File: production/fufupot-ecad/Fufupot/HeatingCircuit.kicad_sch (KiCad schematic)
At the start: 0 parts

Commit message: Heating Schematic Finished
heating schematic finished
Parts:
- added C1: 3.3 uF 275V, symbol Device:C_Polarized
- added C3: 10uF 25V, symbol Device:C_Polarized
- added C4: 0.1uF 63V, symbol Device:C_Polarized
- added C5: 0.37uF 1200V, symbol Device:C_Polarized
- added IC1: FOD3150, DIP762W56P254L966H508Q8N, symbol FOD3150:FOD3150
- added L1: L, symbol Device:L
- added L2: 10uH, symbol Device:L
- added R1: 0.1 5W, symbol Device:R
- added R2: 3.3k, symbol Device:R
- added R3: 10k, symbol Device:R
- added R4: 16, symbol Device:R
- added R5: 330, symbol Device:R
- added U1: STGP8NC60KD, TO-220FP_STM, symbol STGP8NC60KD:STGP8NC60KD
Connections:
- new net: IC1.2 (ANODE), R5.2
- new net: C1.1, C5.1, L1.1, L2.2
- new net: C5.2, L1.2, U1.2 (C)
- new net: C3.2, IC1.5 (VSS), R1.1, R2.1, R3.2, U1.3 (E)
- new net: IC1.6 (VO1), IC1.7 (VO2), R4.1
- new net: R3.1, R4.2, U1.1 (G)
- new net +15V: C3.1, IC1.8 (VDD)
- new net +48V: L2.1
- new net A1: C4.1, R2.2
- new net D9: R5.1
- new net GND: C1.2, C4.2, IC1.3 (CATHODE), R1.2
- no-connect marks 0 -> 2

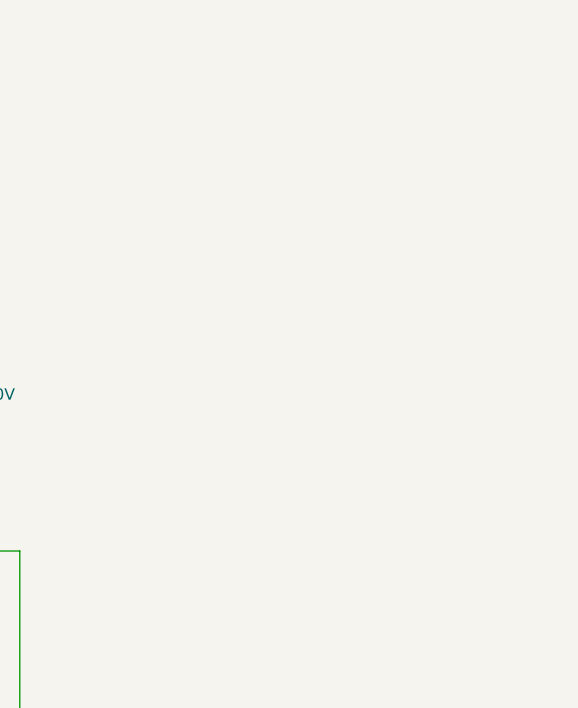
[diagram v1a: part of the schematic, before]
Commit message: Update HeatingCircuit.kicad_sch
Added temp sensing
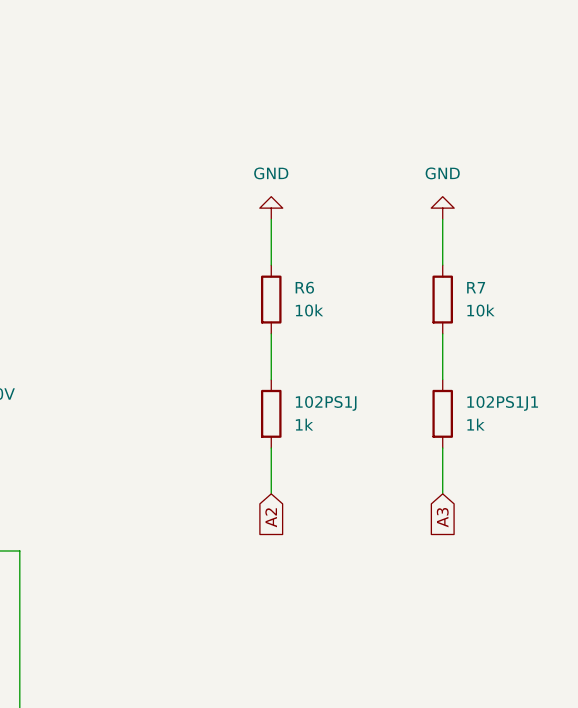
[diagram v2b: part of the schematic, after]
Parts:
- added 102PS1J, 102PS1J1: 1k, symbol Device:R
- added R6, R7: 10k, symbol Device:R
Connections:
- net GND: now also R6.1, R7.1
- new net: 102PS1J1.1, R7.2
- new net: 102PS1J.1, R6.2
- new net A2: 102PS1J.2
- new net A3: 102PS1J1.2
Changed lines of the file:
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@@
+    (stroke (width 0) (type default))
+  )
+  (wire (pts (xy 208.28 77.47) (xy 208.28 82.55))
+    (stroke (width 0) (type default))
+  )
+  (wire (pts (xy 227.33 77.47) (xy 227.33 82.55))
     (stroke (width 0) (type default))
   )
@@
     (stroke (width 0) (type default))
   )
+  (wire (pts (xy 208.28 52.07) (xy 208.28 57.15))
+    (stroke (width 0) (type default))
+  )
   (wire (pts (xy 69.85 107.95) (xy 76.2 107.95))
     (stroke (width 0) (type default))
@@
     (stroke (width 0) (type default))
   )
+  (wire (pts (xy 227.33 52.07) (xy 227.33 57.15))
+    (stroke (width 0) (type default))
+  )
   (wire (pts (xy 157.48 29.21) (xy 157.48 36.83))
     (stroke (width 0) (type default))
@@
     (stroke (width 0) (type default))
   )
+  (wire (pts (xy 208.28 64.77) (xy 208.28 69.85))
+    (stroke (width 0) (type default))
+  )
   (wire (pts (xy 151.13 59.69) (xy 157.48 59.69))
     (stroke (width 0) (type default))
   )
+  (wire (pts (xy 227.33 64.77) (xy 227.33 69.85))
+    (stroke (width 0) (type default))
+  )
   (wire (pts (xy 163.83 74.93) (xy 163.83 80.01))
     (stroke (width 0) (type default))
@@
   (wire (pts (xy 110.49 95.25) (xy 106.68 95.25))
     (stroke (width 0) (type default))
+  )
+  (global_label "A3" (shape input) (at 227.33 82.55 270) (fields_autoplaced)
+    (effects (font (size 1.27 1.27)) (justify right))
+    (property "Intersheetrefs" "${INTERSHEET_REFS}" (at 227.33 87.8333 90)
+      (effects (font (size 1.27 1.27)) (justify right) hide)
+    )
   )
   (global_label "A1" (shape input) (at 173.99 129.54 0) (fields_autoplaced)
@@
     (property "Intersheetrefs" "${INTERSHEET_REFS}" (at 47.8753 107.95 0)
       (effects (font (size 1.27 1.27)) (justify right) hide)
+    )
+  )
+  (global_label "A2" (shape input) (at 208.28 82.55 270) (fields_autoplaced)
+    (effects (font (size 1.27 1.27)) (justify right))
+    (property "Intersheetrefs" "${INTERSHEET_REFS}" (at 208.28 87.8333 90)
+      (effects (font (size 1.27 1.27)) (justify right) hide)
+    )
+  )
+  (symbol (lib_id "power:GND") (at 208.28 52.07 180) (unit 1)
+    (in_bom yes) (on_board yes) (dnp no) (fields_autoplaced)
+    (property "Reference" "#PWR07" (at 208.28 45.72 0)
+      (effects (font (size 1.27 1.27)) hide)
+    )
+    (property "Value" "GND" (at 208.28 46.99 0)
+      (effects (font (size 1.27 1.27)))
+    )
+    (property "Footprint" "" (at 208.28 52.07 0)
+      (effects (font (size 1.27 1.27)) hide)
+    )
+    (property "Datasheet" "" (at 208.28 52.07 0)
+      (effects (font (size 1.27 1.27)) hide)
+    )
+    (pin "1")
+    (instances
+      (project "Fufupot"
+        (path "/e8bc21b1-eda8-45a8-be25-55b90339183f/2c87ff15-d4e6-4940-8625-fb8c3cb7c355"
+          (reference "#PWR07") (unit 1)
+        )
+      )
     )
   )
@@
     )
   )
+  (symbol (lib_id "Device:R") (at 227.33 60.96 0) (unit 1)
+    (in_bom yes) (on_board yes) (dnp no) (fields_autoplaced)
+    (property "Reference" "R7" (at 229.87 59.69 0)
+      (effects (font (size 1.27 1.27)) (justify left))
+    )
+    (property "Value" "10k" (at 229.87 62.23 0)
+      (effects (font (size 1.27 1.27)) (justify left))
+    )
+    (property "Footprint" "" (at 225.552 60.96 90)
+      (effects (font (size 1.27 1.27)) hide)
+    )
+    (property "Datasheet" "~" (at 227.33 60.96 0)
+      (effects (font (size 1.27 1.27)) hide)
+    )
+    (pin "1")
+    (pin "2")
+    (instances
+      (project "Fufupot"
+        (path "/e8bc21b1-eda8-45a8-be25-55b90339183f/2c87ff15-d4e6-4940-8625-fb8c3cb7c355"
+          (reference "R7") (unit 1)
+        )
+      )
+    )
+  )
   (symbol (lib_id "Device:R") (at 114.3 107.95 90) (unit 1)
     (in_bom yes) (on_board yes) (dnp no) (fields_autoplaced)
@@
         (path "/e8bc21b1-eda8-45a8-be25-55b90339183f/2c87ff15-d4e6-4940-8625-fb8c3cb7c355"
           (reference "R5") (unit 1)
+        )
+      )
+    )
+  )
+  (symbol (lib_id "Device:R") (at 208.28 60.96 0) (unit 1)
+    (in_bom yes) (on_board yes) (dnp no) (fields_autoplaced)
+    (property "Reference" "R6" (at 210.82 59.69 0)
+      (effects (font (size 1.27 1.27)) (justify left))
+    )
+    (property "Value" "10k" (at 210.82 62.23 0)
+      (effects (font (size 1.27 1.27)) (justify left))
+    )
+    (property "Footprint" "" (at 206.502 60.96 90)
+      (effects (font (size 1.27 1.27)) hide)
+    )
+    (property "Datasheet" "~" (at 208.28 60.96 0)
+      (effects (font (size 1.27 1.27)) hide)
+    )
+    (pin "1")
+    (pin "2")
+    (instances
+      (project "Fufupot"
+        (path "/e8bc21b1-eda8-45a8-be25-55b90339183f/2c87ff15-d4e6-4940-8625-fb8c3cb7c355"
+          (reference "R6") (unit 1)
         )
       )
@@
         )
       )
+    )
+  )
+  (symbol (lib_id "Device:R") (at 227.33 73.66 0) (unit 1)
+    (in_bom yes) (on_board yes) (dnp no) (fields_autoplaced)
+    (property "Reference" "102PS1J1" (at 229.87 72.39 0)
+      (effects (font (size 1.27 1.27)) (justify left))
+    )
+    (property "Value" "1k" (at 229.87 74.93 0)
+      (effects (font (size 1.27 1.27)) (justify left))
+    )
+    (property "Footprint" "" (at 225.552 73.66 90)
+      (effects (font (size 1.27 1.27)) hide)
+    )
+    (property "Datasheet" "~" (at 227.33 73.66 0)
+      (effects (font (size 1.27 1.27)) hide)
+    )
+    (pin "1")
+    (pin "2")
+    (instances
+      (project "Fufupot"
+        (path "/e8bc21b1-eda8-45a8-be25-55b90339183f/2c87ff15-d4e6-4940-8625-fb8c3cb7c355"
+          (reference "102PS1J1") (unit 1)
+        )
+      )
+    )
+  )
+  (symbol (lib_id "Device:R") (at 208.28 73.66 0) (unit 1)
+    (in_bom yes) (on_board yes) (dnp no) (fields_autoplaced)
+    (property "Reference" "102PS1J" (at 210.82 72.39 0)
+      (effects (font (size 1.27 1.27)) (justify left))
+    )
+    (property "Value" "1k" (at 210.82 74.93 0)
+      (effects (font (size 1.27 1.27)) (justify left))
+    )
+    (property "Footprint" "" (at 206.502 73.66 90)
+      (effects (font (size 1.27 1.27)) hide)
+    )
+    (property "Datasheet" "~" (at 208.28 73.66 0)
+      (effects (font (size 1.27 1.27)) hide)
+    )
+    (pin "1")
+    (pin "2")
+    (instances
+      (project "Fufupot"
+        (path "/e8bc21b1-eda8-45a8-be25-55b90339183f/2c87ff15-d4e6-4940-8625-fb8c3cb7c355"
+          (reference "102PS1J") (unit 1)
+        )
+      )
+    )
+  )
+  (symbol (lib_id "power:GND") (at 227.33 52.07 180) (unit 1)
+    (in_bom yes) (on_board yes) (dnp no) (fields_autoplaced)
+    (property "Reference" "#PWR08" (at 227.33 45.72 0)
+      (effects (font (size 1.27 1.27)) hide)
+    )
+    (property "Value" "GND" (at 227.33 46.99 0)
+      (effects (font (size 1.27 1.27)))
+    )
+    (property "Footprint" "" (at 227.33 52.07 0)
+      (effects (font (size 1.27 1.27)) hide)
+    )
+    (property "Datasheet" "" (at 227.33 52.07 0)
+      (effects (font (size 1.27 1.27)) hide)
+    )
+    (pin "1")
+    (instances
+      (project "Fufupot"
+        (path "/e8bc21b1-eda8-45a8-be25-55b90339183f/2c87ff15-d4e6-4940-8625-fb8c3cb7c355"
+          (reference "#PWR08") (unit 1)
+        )
+      )

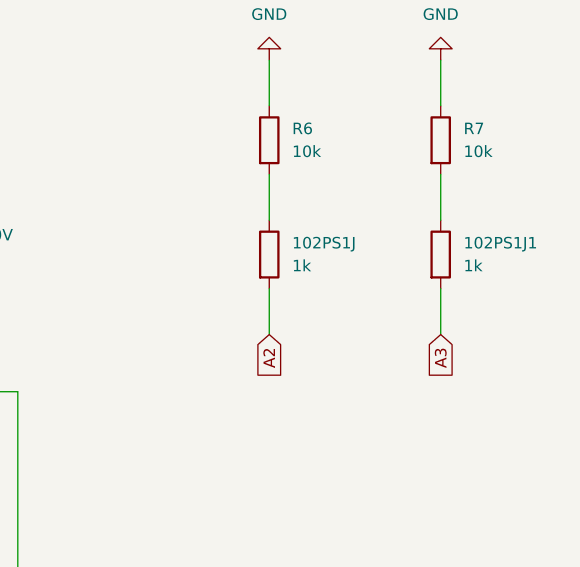
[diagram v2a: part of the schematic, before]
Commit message: Update HeatingCircuit.kicad_sch
Heating and temp sensing fixed
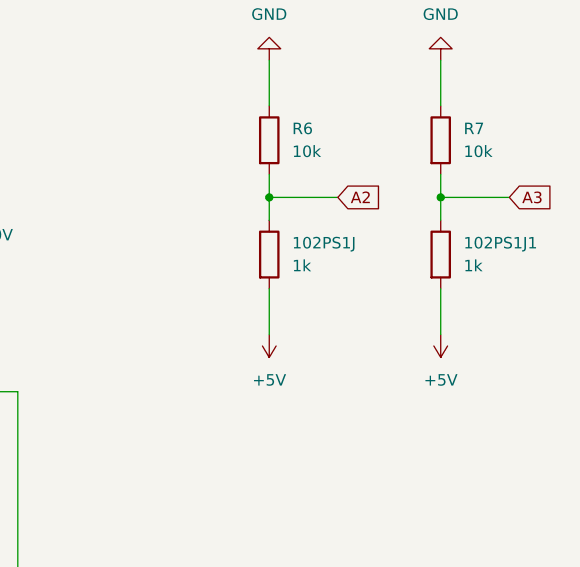
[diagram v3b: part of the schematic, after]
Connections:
- net A2: now also 102PS1J.1, R6.2; no longer 102PS1J.2
- net A3: now also 102PS1J1.1, R7.2; no longer 102PS1J1.2
- new net +5V: 102PS1J.2, 102PS1J1.2

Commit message: Updates unfinished
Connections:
- net A1 renamed A1_Heating
- net D9 renamed D_Heating
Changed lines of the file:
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@@
     )
   )
-  (global_label "A1" (shape input) (at 173.99 129.54 0) (fields_autoplaced)
+  (global_label "A1_Heating" (shape input) (at 173.99 129.54 0) (fields_autoplaced)
     (effects (font (size 1.27 1.27)) (justify left))
-    (property "Intersheetrefs" "${INTERSHEET_REFS}" (at 179.2733 129.54 0)
+    (property "Intersheetrefs" "${INTERSHEET_REFS}" (at 187.4375 129.54 0)
       (effects (font (size 1.27 1.27)) (justify left) hide)
     )
   )
-  (global_label "D9" (shape input) (at 53.34 107.95 180) (fields_autoplaced)
+  (global_label "D_Heating" (shape input) (at 53.34 107.95 180) (fields_autoplaced)
     (effects (font (size 1.27 1.27)) (justify right))
-    (property "Intersheetrefs" "${INTERSHEET_REFS}" (at 47.8753 107.95 0)
+    (property "Intersheetrefs" "${INTERSHEET_REFS}" (at 40.9206 107.95 0)
       (effects (font (size 1.27 1.27)) (justify right) hide)
     )
